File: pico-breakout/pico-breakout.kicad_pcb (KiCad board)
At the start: 2 copper layers, 44 x 59 mm, 8 parts, among them J1 Conn_01x20, J2 Conn_01x20, J3 Conn_01x20, J4 Conn_01x20, J5 Conn_01x03, J6 Conn_01x03

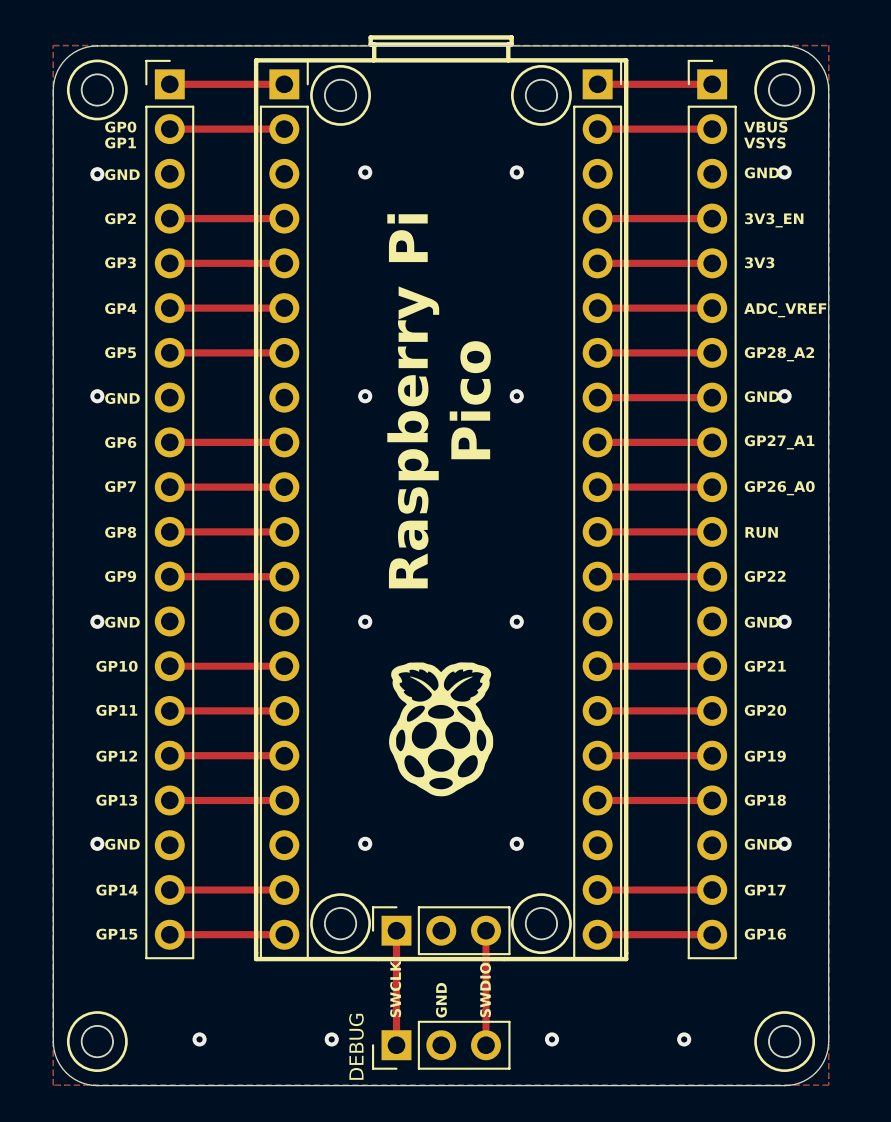
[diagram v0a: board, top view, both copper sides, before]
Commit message: Add series resistor to GPIO 2
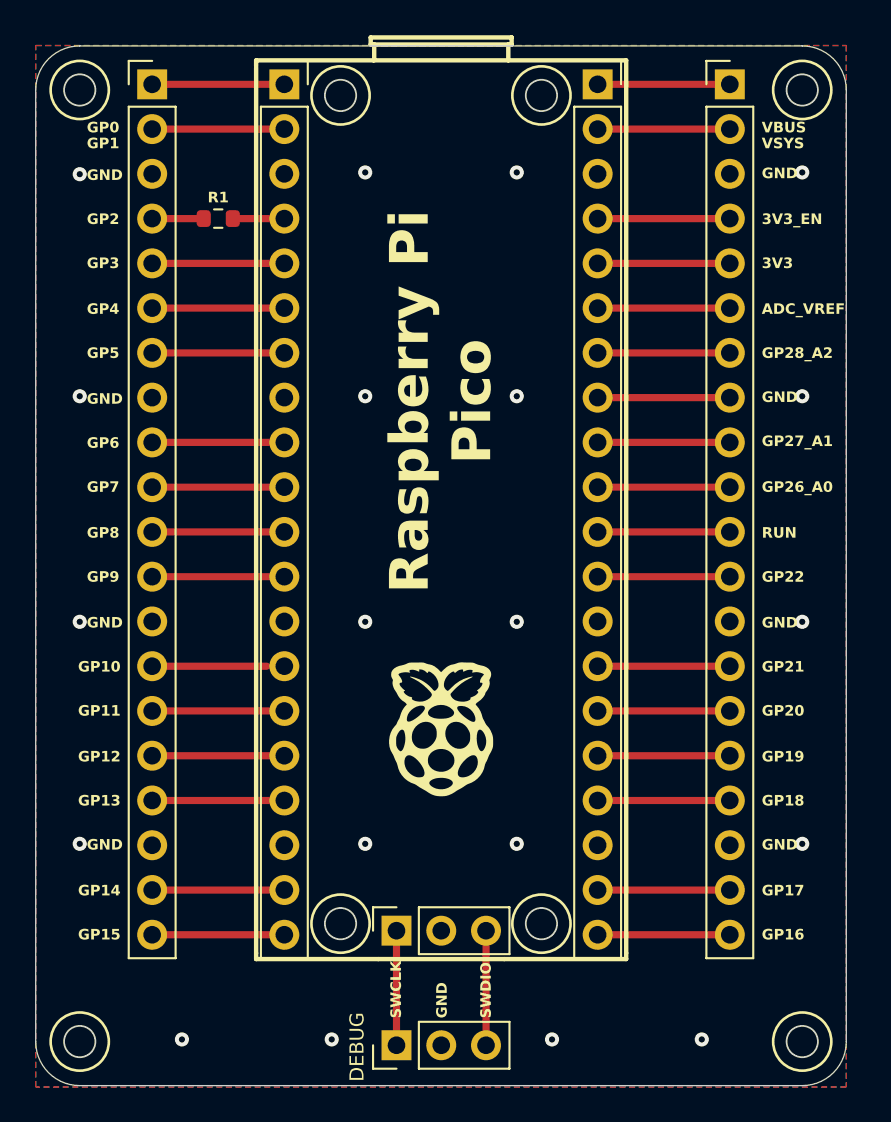
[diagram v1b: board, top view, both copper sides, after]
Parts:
- added R1: 10, Resistor_SMD:R_0603_1608Metric, F.Cu at (47.2, 47.7)
- moved J1 1.00 mm to (43.4, 40.1)
- moved J4 1.00 mm to (76.2, 40.1)
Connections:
- J2 pad 4: Net-(J1-Pin_4) -> Net-(J2-Pin_4)
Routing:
- net Net-(J1-Pin_4): track 6.50 -> 2.93 mm
- net Net-(J2-Pin_4): track 0.00 -> 2.92 mm
- net Net-(J3-Pin_9): track 6.50 -> 7.50 mm
- net Net-(J3-Pin_8): track 6.50 -> 7.50 mm
- net Net-(J3-Pin_7): track 6.50 -> 7.50 mm
- net Net-(J3-Pin_6): track 6.50 -> 7.50 mm
- net Net-(J3-Pin_5): track 6.50 -> 7.50 mm
- net Net-(J3-Pin_4): track 6.50 -> 7.50 mm
- net Net-(J3-Pin_20): track 6.50 -> 7.50 mm
- net Net-(J3-Pin_2): track 6.50 -> 7.50 mm
- net Net-(J3-Pin_19): track 6.50 -> 7.50 mm
- net Net-(J3-Pin_17): track 6.50 -> 7.50 mm
- net Net-(J3-Pin_16): track 6.50 -> 7.50 mm
- net Net-(J3-Pin_15): track 6.50 -> 7.50 mm
- net Net-(J3-Pin_14): track 6.50 -> 7.50 mm
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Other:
- board size 44 x 59 mm -> 46 x 59 mm
- board text added: "Pico Breakout Rev. 1"
- board text removed: "Pico Breakout Rev.1"

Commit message: Final update to Pico breakout boards
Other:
- board text added: "AGND"
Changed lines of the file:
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@@
 		)
 	)
-	(gr_text "GND"
-		(at 73.4 58.2 0)
+	(gr_text "AGND"
+		(at 73.7 58.2 0)
 		(layer "B.SilkS")
 		(effects
@@
 		)
 	)
-	(gr_text "GND"
+	(gr_text "AGND"
 		(at 78 58.2 0)
 		(layer "F.SilkS")
